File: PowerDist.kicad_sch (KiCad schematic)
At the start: 16 parts, among them J7 PowerConn, Q1 Q_PMOS_GSD, U2 RI3-1205S, U3 LD1117-3.3_SOT223

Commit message: basic inputs
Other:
- note removed: "***add mosfet power protection!!!"
- moved on the sheet: C21, C22, C23, D1, D13, J7, Q1, R32, R5, TP1, TP2, TP3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

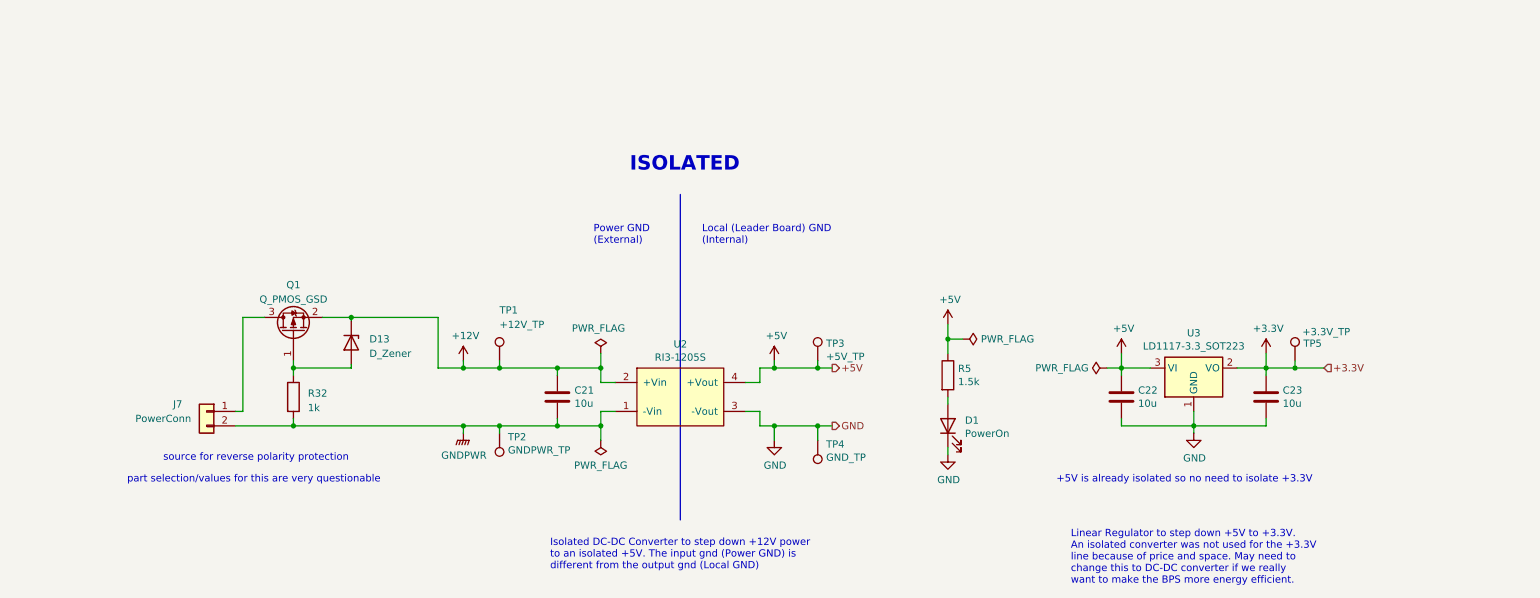
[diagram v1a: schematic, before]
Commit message: switch changes, some caps, annotations
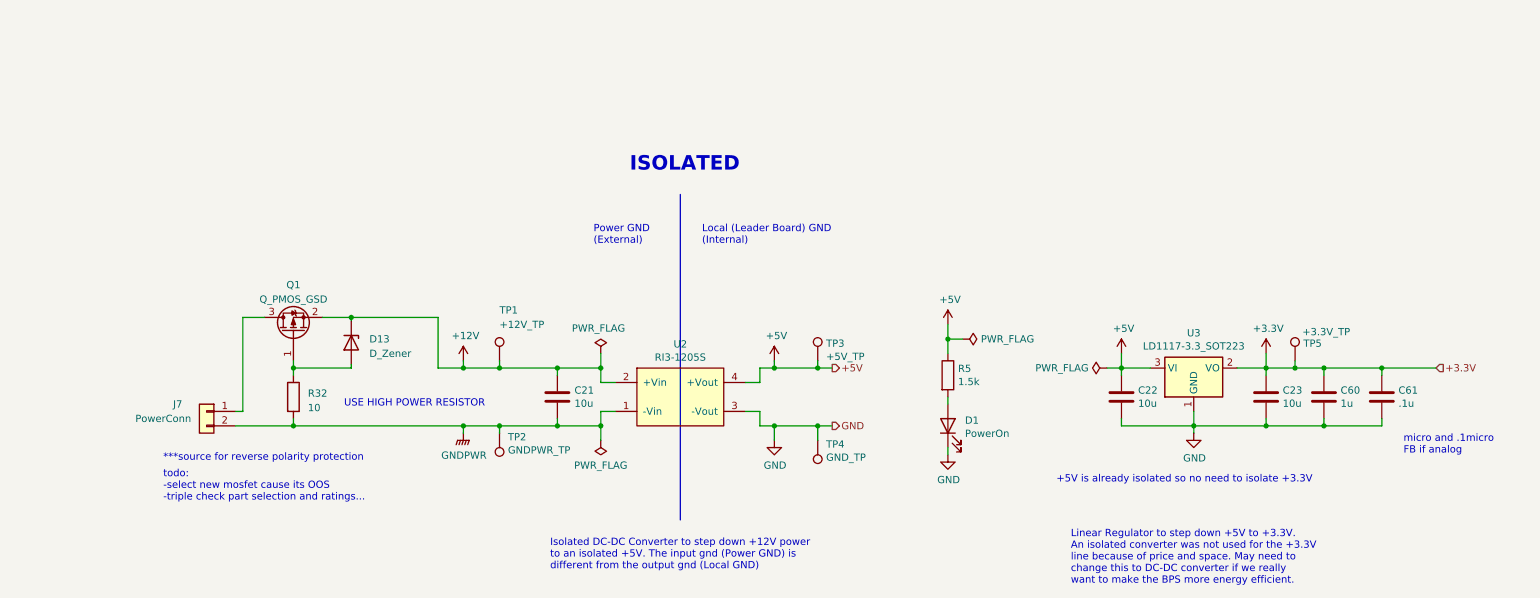
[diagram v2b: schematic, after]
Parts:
- added C60: 1u, Capacitor_SMD:C_0805_2012Metric, symbol Device:C
- added C61: .1u, Capacitor_SMD:C_0805_2012Metric, symbol Device:C
- R32: value 1k -> 10
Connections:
- net +3.3V: now also C60.1, C61.1
- net GND: now also C60.2, C61.2
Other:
- note added: "***source for reverse polarity protection"
- note added: "USE HIGH POWER RESISTOR"
- note added: "micro and .1micro FB if analog"
- note added: "todo: -select new mosfet cause its OOS -triple check part selection and ratings..."
- note removed: "part selection/values for this are very questionable"
- note removed: "source for reverse polarity protection"
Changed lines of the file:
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@@
   (junction (at 102.87 84.455) (diameter 0) (color 0 0 0 0)
   )
+  (junction (at 237.49 94.615) (diameter 0) (color 0 0 0 0)
+  )
+  (junction (at 257.81 84.455) (diameter 0) (color 0 0 0 0)
+  )
   (junction (at 181.61 79.375) (diameter 0) (color 0 0 0 0)
   )
@@
   (junction (at 224.79 94.615) (diameter 0) (color 0 0 0 0)
   )
+  (junction (at 247.65 94.615) (diameter 0) (color 0 0 0 0)
+  )
   (junction (at 212.09 84.455) (diameter 0) (color 0 0 0 0)
   )
   (junction (at 158.75 94.615) (diameter 0) (color 0 0 0 0)
   )
+  (junction (at 247.65 84.455) (diameter 0) (color 0 0 0 0)
+  )
   (junction (at 96.52 84.455) (diameter 0) (color 0 0 0 0)
   )
@@
     (stroke (width 0) (type default))
   )
+  (wire (pts (xy 267.335 84.455) (xy 257.81 84.455))
+    (stroke (width 0) (type default))
+  )
+  (wire (pts (xy 224.79 92.075) (xy 224.79 94.615))
+    (stroke (width 0) (type default))
+  )
+  (wire (pts (xy 237.49 81.915) (xy 237.49 84.455))
+    (stroke (width 0) (type default))
+  )
+  (wire (pts (xy 181.61 99.695) (xy 181.61 98.425))
+    (stroke (width 0) (type default))
+  )
   (wire (pts (xy 247.65 84.455) (xy 242.57 84.455))
     (stroke (width 0) (type default))
   )
-  (wire (pts (xy 224.79 92.075) (xy 224.79 94.615))
-    (stroke (width 0) (type default))
-  )
-  (wire (pts (xy 237.49 81.915) (xy 237.49 84.455))
-    (stroke (width 0) (type default))
-  )
-  (wire (pts (xy 181.61 99.695) (xy 181.61 98.425))
-    (stroke (width 0) (type default))
-  )
   (wire (pts (xy 181.61 76.835) (xy 181.61 79.375))
     (stroke (width 0) (type default))
@@
     (stroke (width 0) (type default))
   )
+  (wire (pts (xy 257.81 84.455) (xy 257.81 85.725))
+    (stroke (width 0) (type default))
+  )
   (wire (pts (xy 148.59 94.615) (xy 151.13 94.615))
     (stroke (width 0) (type default))
@@
     (stroke (width 0) (type default))
   )
+  (wire (pts (xy 247.65 84.455) (xy 247.65 85.725))
+    (stroke (width 0) (type default))
+  )
   (wire (pts (xy 92.075 75.565) (xy 92.075 84.455))
     (stroke (width 0) (type default))
@@
     (stroke (width 0) (type default))
   )
+  (wire (pts (xy 257.81 94.615) (xy 257.81 93.345))
+    (stroke (width 0) (type default))
+  )
   (wire (pts (xy 57.785 92.075) (xy 56.515 92.075))
     (stroke (width 0) (type default))
@@
     (stroke (width 0) (type default))
   )
+  (wire (pts (xy 247.65 94.615) (xy 257.81 94.615))
+    (stroke (width 0) (type default))
+  )
   (wire (pts (xy 102.87 84.455) (xy 113.03 84.455))
     (stroke (width 0) (type default))
   )
+  (wire (pts (xy 257.81 84.455) (xy 247.65 84.455))
+    (stroke (width 0) (type default))
+  )
   (wire (pts (xy 148.59 86.995) (xy 148.59 84.455))
     (stroke (width 0) (type default))
@@
     (stroke (width 0) (type default))
   )
+  (wire (pts (xy 247.65 94.615) (xy 247.65 93.345))
+    (stroke (width 0) (type default))
+  )
   (wire (pts (xy 242.57 84.455) (xy 237.49 84.455))
     (stroke (width 0) (type default))
@@
     (stroke (width 0) (type default))
   )
+  (wire (pts (xy 237.49 94.615) (xy 247.65 94.615))
+    (stroke (width 0) (type default))
+  )
   (wire (pts (xy 209.55 84.455) (xy 212.09 84.455))
     (stroke (width 0) (type default))
@@
   )
   (text "Power GND\n(External)" (at 119.38 62.865 0)
+    (effects (font (size 1.27 1.27)) (justify left bottom))
+  )
+  (text "micro and .1micro\nFB if analog" (at 261.62 99.695 0)
+    (effects (font (size 1.27 1.27)) (justify left bottom))
+  )
+  (text "USE HIGH POWER RESISTOR" (at 75.565 91.44 0)
     (effects (font (size 1.27 1.27)) (justify left bottom))
   )
@@
     (effects (font (size 2.54 2.54) (thickness 0.508) bold) (justify left bottom))
   )
-  (text "part selection/values for this are very questionable"
-    (at 37.465 104.775 0)
+  (text "todo:\n-select new mosfet cause its OOS\n-triple check part selection and ratings..."
+    (at 43.815 107.95 0)
     (effects (font (size 1.27 1.27)) (justify left bottom))
   )
-  (text "source for reverse polarity protection" (at 43.815 100.965 0)
-    (effects (font (size 1.27 1.27)) (justify left bottom) (href "https://www.monolithicpower.com/designing-a-reverse-polarity-protection-circuit-part-i"))
+  (text "***source for reverse polarity protection" (at 43.815 100.965 0)
+    (effects (font (size 1.27 1.27)) (justify left bottom) (href "https://components101.com/articles/design-guide-pmos-mosfet-for-reverse-voltage-polarity-protection"))
   )
   (text "+5V is already isolated so no need to isolate +3.3V"
@@
     (effects (font (size 1.27 1.27)) (justify left))
   )
-  (hierarchical_label "+3.3V" (shape input) (at 247.65 84.455 0) (fields_autoplaced)
+  (hierarchical_label "+3.3V" (shape input) (at 267.335 84.455 0) (fields_autoplaced)
     (effects (font (size 1.27 1.27)) (justify left))
   )
@@
       (effects (font (size 1.27 1.27)) (justify left))
     )
-    (property "Value" "1k" (at 69.215 91.44 0)
+    (property "Value" "10" (at 69.215 91.44 0)
       (effects (font (size 1.27 1.27)) (justify left))
     )
@@
     )
   )
+  (symbol (lib_id "Device:C") (at 247.65 89.535 0) (unit 1)
+    (in_bom yes) (on_board yes) (dnp no)
+    (property "Reference" "C60" (at 250.571 88.3666 0)
+      (effects (font (size 1.27 1.27)) (justify left))
+    )
+    (property "Value" "1u" (at 250.571 90.678 0)
+      (effects (font (size 1.27 1.27)) (justify left))
+    )
+    (property "Footprint" "Capacitor_SMD:C_0805_2012Metric" (at 248.6152 93.345 0)
+      (effects (font (size 1.27 1.27)) hide)
+    )
+    (property "Datasheet" "https://www.mouser.com/datasheet/2/40/AVX_X7RDielectric_777024-1853642.pdf" (at 247.65 89.535 0)
+      (effects (font (size 1.27 1.27)) hide)
+    )
+    (property "P/N" "0805YC106KAT2A" (at 247.65 89.535 0)
+      (effects (font (size 1.27 1.27)) hide)
+    )
+    (pin "1")
+    (pin "2")
+    (instances
+      (project "Telemetry-Primary"
+        (path "/7f2a449b-14af-42b3-8d38-5f0f8a5ee7ce/00000000-0000-0000-0000-00005f6cdfd6"
+          (reference "C60") (unit 1)
+        )
+      )
+    )
+  )
   (symbol (lib_id "power:PWR_FLAG") (at 120.65 81.915 0) (unit 1)
     (in_bom yes) (on_board yes) (dnp no)
@@
         )
       )
+    )
+  )
+  (symbol (lib_id "Device:C") (at 257.81 89.535 0) (unit 1)
+    (in_bom yes) (on_board yes) (dnp no)
+    (property "Reference" "C61" (at 260.731 88.3666 0)
+      (effects (font (size 1.27 1.27)) (justify left))
+    )
+    (property "Value" ".1u" (at 260.731 90.678 0)
+      (effects (font (size 1.27 1.27)) (justify left))
+    )
+    (property "Footprint" "Capacitor_SMD:C_0805_2012Metric" (at 258.7752 93.345 0)
+      (effects (font (size 1.27 1.27)) hide)
+    )
+    (property "Datasheet" "https://www.mouser.com/datasheet/2/40/AVX_X7RDielectric_777024-1853642.pdf" (at 257.81 89.535 0)
+      (effects (font (size 1.27 1.27)) hide)
+    )
+    (property "P/N" "0805YC106KAT2A" (at 257.81 89.535 0)
+      (effects (font (size 1.27 1.27)) hide)
+    )
+    (pin "1")
+    (pin "2")
+    (instances
+      (project "Telemetry-Primary"
+        (path "/7f2a449b-14af-42b3-8d38-5f0f8a5ee7ce/00000000-0000-0000-0000-00005f6cdfd6"
+          (reference "C61") (unit 1)
+        )
+      )

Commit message: layout rearranging
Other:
- note removed: "micro and .1micro FB if analog"
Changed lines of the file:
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@@
-    (effects (font (size 1.27 1.27)) (justify left bottom))
-  )
-  (text "micro and .1micro\nFB if analog" (at 261.62 99.695 0)
     (effects (font (size 1.27 1.27)) (justify left bottom))
   )
